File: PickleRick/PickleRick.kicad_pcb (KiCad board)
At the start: 4 copper layers, 100 x 37 mm, 184 parts, among them J1 Conn_01x05_Male, J10 Conn_01x03_Male, J11 Conn_01x03_Male, J12 Conn_01x03_Male, J13 Conn_01x03_Male, J14 DeployLipo, J15 UCLipo, J16 Conn_Coaxial, J17 USB_C_Receptacle_USB2.0, J18 Conn_Coaxial, J2 Conn_01x02_Male, J3 Conn_01x02_Male, J4 Micro_SD_Card_Det, J5 Conn_01x07_Male, Q1 MMDT2222A, Q2 PMV20ENR, Q3 PMV20ENR, Q4 PMV20ENR, Q5 PMV20ENR, Q6 PMV20ENR, U1 SN65HVD230, U10 LTC4411ES5TRMPBF, U11 LTC4411ES5TRMPBF, U12 TPS54233D, U13 LTC4412xS6, U14 LTC4412xS6, U15 LTC4412xS6, U16 LTC4412xS6, U17 MAX-M8Q, U18 CP2102-GMR-QFN28, U19 RFM95W-868S2, U2 ESP32-WROOM-32D, U3 MS5607-02BA, U4 LTV-247, U5 PCA9534RGVR, U6 PCA9685BS, U7 H3LIS100DLTR, U8 ICM-20608-G, U9 MMC5983MA

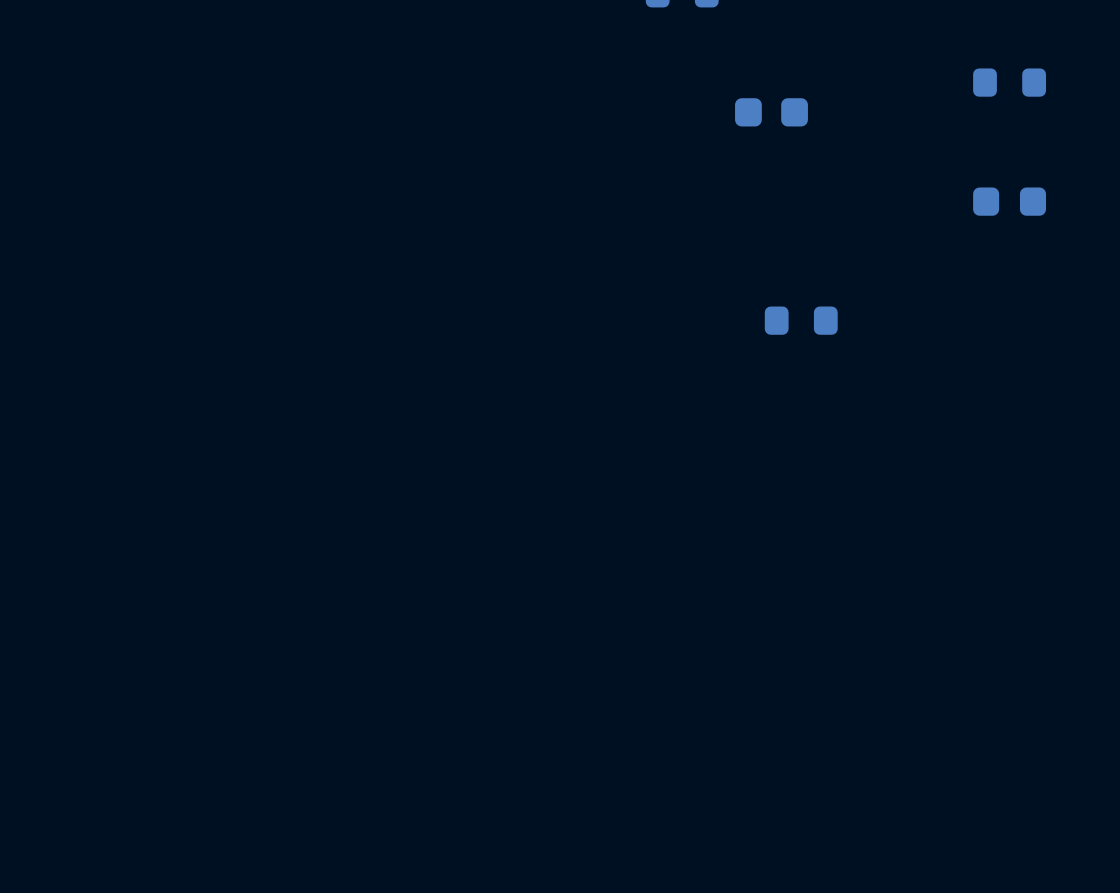
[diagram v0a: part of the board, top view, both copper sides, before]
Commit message: Annotated schematic & done layout for buck converter
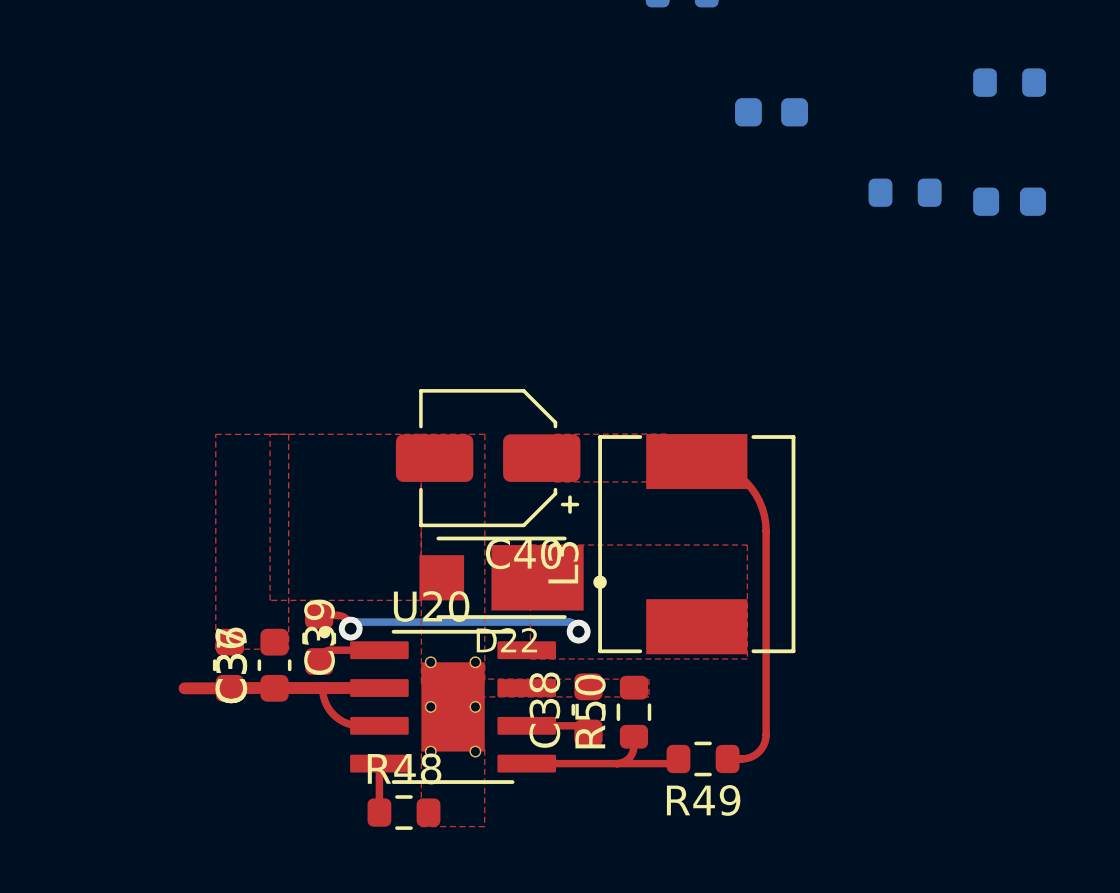
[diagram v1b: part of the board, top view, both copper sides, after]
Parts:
- added C36: 0.1uF, Capacitor_SMD:C_0603_1608Metric, F.Cu at (117.5, 155.4)
- added C37: 10uF, Capacitor_SMD:C_0603_1608Metric, F.Cu at (116.0, 155.4)
- added C38: 22nF, Capacitor_SMD:C_0603_1608Metric, F.Cu at (128.1, 156.9)
- added C39: 0.1uF, Capacitor_SMD:C_0603_1608Metric, F.Cu at (119.0, 154.5)
- added C40: more than 54.2 uF, Capacitor_SMD:CP_Elec_4x5.8, F.Cu at (124.7, 148.4)
- added D22: V8PAM10S, iclr:DIO_V3PAN50-M3_I, F.Cu at (125.1, 152.5)
- added L3: 4.7 uH, iclr:IND_SRP6540-390M, F.Cu at (131.7, 151.3)
- added R48: 49.9k, Resistor_SMD:R_0603_1608Metric, F.Cu at (121.9, 160.4)
- added R49: 64.67k, Resistor_SMD:R_0603_1608Metric, F.Cu at (131.9, 158.6)
- added R50: 10k, Resistor_SMD:R_0603_1608Metric, F.Cu at (129.6, 157.0)
- added U20: LMR14050-Q1, iclr:SOIC127P600X170-9N, F.Cu at (123.5, 156.8)
- moved R38 5.54 mm to (138.7, 139.5)
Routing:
- net +6V: track 0.00 -> 12.1 mm
- net Net-(C39-Pad2): track 0.00 -> 9.52 mm, vias 0 -> 2
- net +24V: track 0.00 -> 9.15 mm
- net /nukes/FB: track 0.00 -> 6.38 mm
- net Net-(C39-Pad1): track 0.00 -> 2.23 mm
- net Net-(C38-Pad1): track 0.00 -> 2.17 mm
- net Net-(R48-Pad1): track 0.00 -> 1.65 mm
- added copper zone on F.Cu, net +6V
- added copper zone on F.Cu, net Net-(C39-Pad2)
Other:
- board text added: "24V IN"

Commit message: first full layout of pickle complete
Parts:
- removed BZ1: Buzzer, Buzzer_Beeper:Buzzer_TDK_PS1240P02BT_D12.2mm_H6.5mm
- removed C40: more than 54.2 uF, Capacitor_SMD:CP_Elec_4x5.8
- removed D13, D14, D7, D9: FIRING, LED_SMD:LED_0603_1608Metric
- removed D22: V8PAM10S, iclr:DIO_V3PAN50-M3_I
- removed G***: LOGO, iclr:iclr_logo
- removed G***: LOGO, iclr:pickle_ric
- removed J13: Conn_01x03_Male, Connector_PinHeader_2.54mm:PinHeader_1x03_P2.54mm_Vertical
- removed L1: PE-92111KNL, Inductor_SMD:L_12x12mm_H6mm
- removed L3: 4.7 uH, iclr:IND_SRP6540-390M
- removed R23, R24, R31, R32: 2K, Resistor_SMD:R_0603_1608Metric
- removed R50: 10k, Resistor_SMD:R_0603_1608Metric
- removed REF**: Write_Pad, iclr:Write_Pad
- removed REF**: Axes_Magnetic_Lefthand_Xdown, iclr:Axes_Magnetic_Lefthand_Xdown
- removed TP1, TP10, TP2, TP29, TP4, TP7, TP9: TestPoint, TestPoint:TestPoint_THTPad_1.0x1.0mm_Drill0.5mm
- removed U20: LMR14050-Q1, iclr:SOIC127P600X170-9N
- added D21: USB_LED, LED_SMD:LED_0603_1608Metric, F.Cu at (168.3, 94.9)
- added J6: Screw_Terminal_01x08, TerminalBlock_TE-Connectivity:TerminalBlock_TE_282834-8_1x08_P2.54mm_Horizontal, F.Cu at (119.5, 62.3)
- added JP1: SolderJumper_2_Open, Jumper:SolderJumper-2_P1.3mm_Open_RoundedPad1.0x1.5mm, F.Cu at (173.9, 65.2)
- added JP2: SolderJumper_2_Open, Jumper:SolderJumper-2_P1.3mm_Open_RoundedPad1.0x1.5mm, B.Cu at (148.0, 66.4)
- added Q10: AO3401A, Package_TO_SOT_SMD:SOT-23, F.Cu at (156.4, 88.1)
- added Q7: SI4143DY-T1-GE3, Package_SO:SOIC-8_3.9x4.9mm_P1.27mm, F.Cu at (136.5, 70.7)
- added Q8: SI4143DY-T1-GE3, Package_SO:SOIC-8_3.9x4.9mm_P1.27mm, F.Cu at (145.9, 71.5)
- added Q9: AO3401A, Package_TO_SOT_SMD:SOT-23, F.Cu at (151.3, 85.3)
- C23: value 10 nF -> 10uF
- C24: value 130pF -> 10uF
- C26: value 130pF -> 100nF
- C27: value 0.1uF -> 160pF
- C28: value 470uF -> 100nF; footprint Capacitor_SMD:CP_Elec_8x6.7 -> Capacitor_SMD:C_0603_1608Metric
- C36: value 0.1uF -> 10uF
- C37: value 10uF -> 0.1uF
- C38: value 22nF -> 220pF
- C39: value 0.1uF -> 220 pF
- D10, D15, D16, D8: footprint Diode_SMD:D_SOD-123F -> Diode_SMD:D_SOD-128
- D19: value B340 -> SM712_SOT23; footprint Diode_SMD:D_SMC -> Package_TO_SOT_SMD:SOT-23
- D6, J5, Q2, R10, R11, R16, R22, R9: moved to B.Cu
- J1: value Conn_01x05_Male -> Conn_01x06_Male; footprint Connector_PinSocket_2.54mm:PinSocket_1x05_P2.54mm_Vertical -> Connector_Molex:Molex_Mini-Fit_Jr_5566-06A_2x03_P4.20mm_Vertical
- J11: value Conn_01x03_Male -> Conn_01x02_Male; footprint Connector_PinHeader_2.54mm:PinHeader_1x03_P2.54mm_Vertical -> Connector_JST:JST_PH_B2B-PH-K_1x02_P2.00mm_Vertical
- J12: value Conn_01x03_Male -> Conn_01x05_Male; footprint Connector_PinHeader_2.54mm:PinHeader_1x03_P2.54mm_Vertical -> Connector_PinHeader_2.54mm:PinHeader_1x05_P2.54mm_Vertical
- J14: footprint TerminalBlock_Phoenix:TerminalBlock_Phoenix_MKDS-1,5-2-5.08_1x02_P5.08mm_Horizontal -> TerminalBlock_Phoenix:TerminalBlock_Phoenix_MKDS-3-2-5.08_1x02_P5.08mm_Horizontal
- J15: footprint TerminalBlock_Phoenix:TerminalBlock_Phoenix_MKDS-1,5-2-5.08_1x02_P5.08mm_Horizontal -> Connector_JST:JST_PH_B2B-PH-K_1x02_P2.00mm_Vertical
- J4, R15: moved to F.Cu
- Q3, Q4, Q5, Q6: value PMV20ENR -> NCV8415STT1G; footprint Package_TO_SOT_SMD:SOT-23 -> Package_TO_SOT_SMD:SOT-223
- R39: value 54.9K -> 90
- R40: value 10K -> 90
- R41: value 1.54K -> 10k
- R48: value 49.9k -> 60
- R49: value 64.67k -> 60
- TP11, TP12, TP13, TP14, TP15, TP16, TP20, TP21, TP22, TP23, TP24, TP25, TP26, TP27, TP28, TP3, TP5, TP6, TP8: footprint TestPoint:TestPoint_THTPad_1.0x1.0mm_Drill0.5mm -> TestPoint:TestPoint_Pad_D1.0mm
- TP17, TP18, TP19, TP30, TP31, TP32: footprint TestPoint:TestPoint_THTPad_1.0x1.0mm_Drill0.5mm -> TestPoint:TestPoint_Pad_D1.0mm; moved to B.Cu
- U12: value TPS54233D -> LT1963AxST-3.3; footprint iclr:SOIC127P599X175-8N -> Package_TO_SOT_SMD:SOT-223-3_TabPin2
- moved TP20 157.7 mm to (187.8, 67.9)
- moved TP8 154.9 mm to (193.8, 90.7)
- moved TP26 153.4 mm to (190.2, 68.1)
- moved TP23 153.2 mm to (183.8, 65.4)
- moved TP25 149.9 mm to (192.3, 68.1)
- moved TP21 148.7 mm to (185.8, 67.9)
- moved D6 143.5 mm to (188.6, 66.0), turned to 90 degrees
- moved TP24 141.2 mm to (183.8, 67.9)
- moved TP3 140.2 mm to (191.3, 66.4)
- moved Q2 138.7 mm to (185.4, 66.5)
- moved TP16 136.9 mm to (171.9, 76.0)
- moved TP14 133.0 mm to (177.2, 83.0)
- moved TP13 133.0 mm to (168.3, 83.7)
- moved TP6 129.8 mm to (188.3, 91.4)
- moved TP15 129.4 mm to (166.5, 84.8)
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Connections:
- net Net-(J14-Pad1) renamed /power/Deploy_Lipo+
- net Net-(J15-Pad1) renamed /power/UC_Lipo+
- C23 pad 1: Net-(C23-Pad1) -> +3V3
- C24 pad 1: Net-(C24-Pad1) -> GND
- C24 pad 2: GND -> /power/3.3reg_in
- C25 pad 1: +24V -> GND
- C25 pad 2: GND -> /power/3.3reg_out
- C26 pad 1: Net-(C24-Pad1) -> GND
- C26 pad 2: Net-(C26-Pad2) -> /power/3.3reg_out
- C27 pad 1: Net-(C27-Pad1) -> GND
- C28 pad 1: +6V -> +3V3
- C36 pad 1: +24V -> +3V3
- C37 pad 1: +24V -> Net-(C37-Pad1)
- C38 pad 1: Net-(C38-Pad1) -> GND
- C38 pad 2: GND -> /CAN_HIGH
- C39 pad 1: Net-(C39-Pad1) -> GND
- C39 pad 2: Net-(C39-Pad2) -> /CAN_LOW
- C7 pad 2: Net-(C7-Pad2) -> GND
- C8 pad 2: Net-(C7-Pad2) -> GND
- D10 pad 2: Net-(D10-Pad2) -> /nukes/Nuke3-
- D11 pad 2: Net-(D11-Pad2) -> /nukes/Nuke1-
- D12 pad 2: Net-(D10-Pad2) -> /nukes/Nuke3-
- D15 pad 2: Net-(D15-Pad2) -> /nukes/Nuke2-
- D16 pad 2: Net-(D16-Pad2) -> /nukes/Nuke4-
- D17 pad 2: Net-(D15-Pad2) -> /nukes/Nuke2-
- D18 pad 2: Net-(D16-Pad2) -> /nukes/Nuke4-
- D19 pad 1: Net-(C27-Pad2) -> /CAN_LOW
- D19 pad 2: GND -> /CAN_HIGH
- D6 pad 2: Net-(BZ1-Pad2) -> Net-(D6-Pad2)
- D8 pad 2: Net-(D11-Pad2) -> /nukes/Nuke1-
- J1 pad 1: /CAN_HIGH -> GND
- J1 pad 3: /power/RBUS_24V_IN -> /power/RBUS_3.3_IN
- J1 pad 4: /power/RBUS_3.3_IN -> /power/RBUS_24V_IN
- J1 pad 5: /CAN_LOW -> /CAN_HIGH
- J10 pad 2: +6V -> /SCL
- J10 pad 3: /nukes/SERVO1 -> /SDA
- J11 pad 1: GND -> Net-(D6-Pad2)
- J11 pad 2: +6V -> +3V3
- J12 pad 2: +6V -> /nukes/SERVO1
- J12 pad 3: /nukes/SERVO3 -> /nukes/SERVO2
- Q3 pad 2: GND -> Net-(D8-Pad1)
- Q3 pad 3: Net-(D8-Pad1) -> GND
- Q4 pad 2: GND -> Net-(D10-Pad1)
- Q4 pad 3: Net-(D10-Pad1) -> GND
- Q5 pad 2: GND -> Net-(D15-Pad1)
- Q5 pad 3: Net-(D15-Pad1) -> GND
- Q6 pad 2: GND -> Net-(D16-Pad1)
- Q6 pad 3: Net-(D16-Pad1) -> GND
- R36 pad 1: Net-(R36-Pad1) -> Net-(U4-Pad1)
- R39 pad 1: Net-(C26-Pad2) -> /CAN_TX
- R39 pad 2: GND -> Net-(C27-Pad2)
- R40 pad 1: +6V -> /CAN_RX
- R40 pad 2: /power/VSENSE -> Net-(R40-Pad2)
- R41 pad 1: /power/VSENSE -> Net-(R41-Pad1)
- R48 pad 1: Net-(R48-Pad1) -> /CAN_HIGH
- R48 pad 2: GND -> Net-(C37-Pad1)
- R49 pad 1: +6V -> Net-(C37-Pad1)
- R49 pad 2: /nukes/FB -> /CAN_LOW
- TP11 pad 1: /HSPI_MISO -> /VSPI_MISO
- TP12 pad 1: /HSPI_MOSI -> /VSPI_MOSI
- TP13 pad 1: /HSPI_SCLK -> /VSPI_SCLK
- TP17 pad 1: /VSPI_SCLK -> /HSPI_SCLK
- TP18 pad 1: /VSPI_MISO -> /HSPI_MISO
- TP19 pad 1: /VSPI_MOSI -> /HSPI_MOSI
- U1 pad 1: /CAN_TX -> Net-(C27-Pad2)
- U1 pad 4: /CAN_RX -> Net-(R40-Pad2)
- U1 pad 5: unconnected-(U1-Pad5) -> /Vref
- U1 pad 8: GND -> Net-(R41-Pad1)
- U12 pad 1: Net-(C27-Pad1) -> /power/3.3reg_in
- U12 pad 2: +24V -> GND
- U12 pad 3: unconnected-(U12-Pad3) -> /power/3.3reg_out
- U13 pad 5: unconnected-(U13-Pad5) -> Net-(Q7-Pad4)
- U13 pad 6: unconnected-(U13-Pad6) -> +24V
- U14 pad 5: unconnected-(U14-Pad5) -> Net-(Q8-Pad4)
- U14 pad 6: unconnected-(U14-Pad6) -> +24V
- U15 pad 5: unconnected-(U15-Pad5) -> Net-(Q9-Pad1)
- U15 pad 6: unconnected-(U15-Pad6) -> /power/3.3reg_in
- U16 pad 5: unconnected-(U16-Pad5) -> Net-(Q10-Pad1)
- U16 pad 6: unconnected-(U16-Pad6) -> /power/3.3reg_in
- U2 pad 12: /BARO_CS -> /Buzzer
- U2 pad 13: /HSPI_SCLK -> /VSPI_SCLK
- U2 pad 14: /HSPI_MISO -> /VSPI_MISO
- U2 pad 16: /HSPI_MOSI -> /VSPI_MOSI
- U2 pad 24: /Buzzer -> /BARO_CS
- U2 pad 30: /VSPI_SCLK -> /HSPI_SCLK
- U2 pad 31: /VSPI_MISO -> /HSPI_MISO
- U2 pad 37: /VSPI_MOSI -> /HSPI_MOSI
- U4 pad 1: Net-(R27-Pad1) -> Net-(U4-Pad1)
- U4 pad 10: /nukes/Cont4 -> /nukes/Cont1
- U4 pad 12: /nukes/Cont3 -> /nukes/Cont2
- U4 pad 14: /nukes/Cont2 -> /nukes/Cont3
- U4 pad 16: /nukes/Cont1 -> /nukes/Cont4
- U4 pad 2: Net-(D11-Pad2) -> /nukes/Nuke4-
- U4 pad 3: Net-(R35-Pad1) -> Net-(R29-Pad1)
- U4 pad 4: Net-(D15-Pad2) -> /nukes/Nuke3-
- U4 pad 5: Net-(R29-Pad1) -> Net-(R35-Pad1)
- U4 pad 6: Net-(D10-Pad2) -> /nukes/Nuke2-
- U4 pad 7: Net-(R36-Pad1) -> Net-(R27-Pad1)
- U4 pad 8: Net-(D16-Pad2) -> /nukes/Nuke1-
- U5 pad 10: /nukes/Nuke4 -> /nukes/Nuke1
- U5 pad 2: /nukes/Cont1 -> /nukes/Cont4
- U5 pad 3: /nukes/Nuke1 -> /nukes/Nuke4
- U5 pad 4: /nukes/Cont2 -> /nukes/Cont3
- U5 pad 5: /nukes/Nuke2 -> /nukes/Nuke3
- U5 pad 7: /nukes/Cont3 -> /nukes/Cont2
- U5 pad 8: /nukes/Nuke3 -> /nukes/Nuke2
- U5 pad 9: /nukes/Cont4 -> /nukes/Cont1
- U6 pad 10: unconnected-(U6-Pad10) -> /nukes/SERVO1
- U6 pad 11: Net-(U6-Pad11) -> GND
- U6 pad 12: unconnected-(U6-Pad12) -> /nukes/SERVO2
- U6 pad 13: unconnected-(U6-Pad13) -> /nukes/SERVO3
- U6 pad 14: unconnected-(U6-Pad14) -> /nukes/SERVO4
- U6 pad 29: Net-(U6-Pad11) -> GND
- U6 pad 3: /nukes/SERVO1 -> unconnected-(U6-Pad3)
- U6 pad 4: /nukes/SERVO2 -> unconnected-(U6-Pad4)
- U6 pad 5: /nukes/SERVO3 -> unconnected-(U6-Pad5)
- U6 pad 6: /nukes/SERVO4 -> unconnected-(U6-Pad6)
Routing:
- net GND: track 0.00 -> 231.2 mm, vias 0 -> 104
- net /SDA: track 2.22 -> 133.4 mm, vias 0 -> 3
- net /SCL: track 2.00 -> 131.0 mm, vias 0 -> 2
- net /LORA_INT: track 0.00 -> 110.3 mm, vias 0 -> 1
- net /SD1_DET: track 1.65 -> 110.6 mm, vias 0 -> 3
- net /SD2_CS: track 0.00 -> 99.3 mm, vias 0 -> 3
- net /SD1_CS: track 1.97 -> 100.3 mm, vias 0 -> 2
- net /HSPI_MOSI: track 0.00 -> 97.4 mm, vias 0 -> 2
- net /VSPI_SCLK: track 3.86 -> 99.9 mm, vias 0 -> 6
- net /SD2_DET: track 0.00 -> 96.0 mm, vias 0 -> 2
- net /VSPI_MOSI: track 9.33 -> 98.9 mm, vias 0 -> 6
- net /VSPI_MISO: track 17.4 -> 105.6 mm, vias 0 -> 6
- net /HSPI_MISO: track 0.00 -> 83.2 mm, vias 0 -> 2
- net +3V3: track 12.6 -> 94.3 mm, vias 0 -> 36
- net /HSPI_SCLK: track 0.00 -> 77.7 mm, vias 0 -> 2
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- added copper zone on F.Cu, net +24V
- added copper zone on In2.Cu, net +3V3
- added copper zone on F.Cu, net /power/Deploy_Lipo+
- added copper zone on F.Cu, net /power/RBUS_24V_IN
- added copper zone on In1.Cu, net GND
- removed copper zone on F.Cu, net +6V
- removed copper zone on F.Cu, net Net-(C39-Pad2)
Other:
- board text removed: "24V IN"

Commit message: pickle layed out
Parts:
- removed D11, D12, D17, D18: CONTINUITY, LED_SMD:LED_0603_1608Metric
- removed R28, R30, R37, R38: 2K, Resistor_SMD:R_0603_1608Metric
- removed TP5: TestPoint, TestPoint:TestPoint_Pad_D1.0mm
- added G***: LOGO, iclr:pickle_ric, B.Cu at (167.7, 77.8)
- added LOGO1: LOGO, iclr:iclr_logo, F.Cu at (129.2, 75.2)
- added REF**: Write_Pad, iclr:Write_Pad, F.Cu at (190.9, 78.0)
- added TP1: TestPoint, TestPoint:TestPoint_Pad_D1.0mm, F.Cu at (170.9, 88.0)
- added TP2: TestPoint, TestPoint:TestPoint_Pad_D1.0mm, F.Cu at (177.4, 95.9)
- moved JP2 19.9 mm to (167.9, 65.3), turned to 90 degrees
- moved J10 11.5 mm to (109.1, 61.9)
- moved TP6 5.90 mm to (194.2, 90.8)
- moved TP22 5.53 mm to (159.1, 83.4)
- moved Q6 3.22 mm to (115.3, 72.9)
- moved R36 3.21 mm to (110.7, 81.0), turned to 0 degrees
- moved R27 2.79 mm to (120.2, 81.0), turned to 0 degrees
- moved R35 2.78 mm to (117.2, 81.0), turned to 0 degrees
- moved TP8 2.51 mm to (191.2, 90.8)
- moved C8 2.43 mm to (122.8, 93.0)
- moved Q3 2.29 mm to (138.8, 72.9)
- moved R29 2.29 mm to (113.7, 81.0)
- moved TP13 2.24 mm to (167.8, 81.5)
- moved D16 2.15 mm to (114.8, 66.1)
- moved D10 2.10 mm to (122.7, 66.2)
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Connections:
- J10 pad 2: /SCL -> /SDA
- J10 pad 3: /SDA -> /SCL
- R36 pad 1: Net-(U4-Pad1) -> Net-(R36-Pad1)
- U4 pad 1: Net-(U4-Pad1) -> /nukes/Nuke4-
- U4 pad 10: /nukes/Cont1 -> +3V3
- U4 pad 11: +3V3 -> /nukes/Cont2
- U4 pad 12: /nukes/Cont2 -> +3V3
- U4 pad 13: +3V3 -> /nukes/Cont3
- U4 pad 14: /nukes/Cont3 -> +3V3
- U4 pad 15: +3V3 -> /nukes/Cont4
- U4 pad 16: /nukes/Cont4 -> +3V3
- U4 pad 2: /nukes/Nuke4- -> Net-(R36-Pad1)
- U4 pad 3: Net-(R29-Pad1) -> /nukes/Nuke3-
- U4 pad 4: /nukes/Nuke3- -> Net-(R29-Pad1)
- U4 pad 5: Net-(R35-Pad1) -> /nukes/Nuke2-
- U4 pad 6: /nukes/Nuke2- -> Net-(R35-Pad1)
- U4 pad 7: Net-(R27-Pad1) -> /nukes/Nuke1-
- U4 pad 8: /nukes/Nuke1- -> Net-(R27-Pad1)
- U4 pad 9: +3V3 -> /nukes/Cont1
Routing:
- net GND: track 231.2 -> 160.7 mm, vias 104 -> 266
- net /nukes/Nuke1: track 1.15 -> 45.2 mm, vias 1 -> 2
- net /SCL: track 131.0 -> 161.3 mm
- net /nukes/Nuke2: track 1.69 -> 30.6 mm, vias 1 -> 2
- net /nukes/Nuke4: track 1.40 -> 28.7 mm, vias 1 -> 2
- net /SDA: track 133.4 -> 159.8 mm
- net /nukes/Nuke3: track 1.43 -> 23.9 mm, vias 1 -> 2
- net /power/Deploy_Lipo+: track 8.00 -> 26.1 mm, vias 0 -> 1
- net /power/UC_Lipo+: track 50.5 -> 36.1 mm
- net /LORA_INT: track 110.3 -> 119.1 mm, vias 1 -> 2
- net /nukes/Nuke1-: track 54.2 -> 62.4 mm
- net /nukes/Nuke2-: track 58.4 -> 53.0 mm
- net Net-(D17-Pad1): track 5.15 -> 0.00 mm
- net +3V3: track 94.3 -> 97.9 mm, vias 36 -> 43
- net Net-(R36-Pad1): track 0.00 -> 2.72 mm
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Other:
- outline, holes or cut-outs redrawn
- board text added: "Designed By Kiran de Silva Electronics & Payload 2022"
- board text added: "Pickle Rick V1.0"

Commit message: pickle update
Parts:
- added R23: 7.5k, Resistor_SMD:R_0603_1608Metric, B.Cu at (170.2, 64.5)
- added R24: 2.4k, Resistor_SMD:R_0603_1608Metric, B.Cu at (170.2, 66.0)
- added R28: 24k, Resistor_SMD:R_0603_1608Metric, B.Cu at (170.2, 92.1)
- added R30: 47k, Resistor_SMD:R_0603_1608Metric, B.Cu at (170.2, 93.6)
- J5: value Conn_01x07_Male -> 292227-7; footprint Connector_JST:JST_GH_SM07B-GHS-TB_1x07-1MP_P1.25mm_Horizontal -> iclr:292227-7
- TP2: moved to B.Cu
- moved R16 19.4 mm to (150.3, 91.6), turned to 0 degrees
- moved R21 10.2 mm to (140.7, 84.8), turned to -90 degrees
- moved J5 7.70 mm to (129.0, 88.3), turned to 0 degrees
- moved R22 4.13 mm to (138.7, 84.8)
- moved TP2 1.32 mm to (176.4, 95.1), turned to 180 degrees
- moved TP23 0.94 mm to (184.3, 65.5)
- moved TP1 0.85 mm to (171.0, 87.2)
- moved R10 0.62 mm to (145.2, 94.2)
- moved R9 0.60 mm to (145.2, 95.7)
- moved JP2 0.53 mm to (167.4, 65.2)
- moved R11 0.50 mm to (145.2, 92.6)
- moved JP1 0.38 mm to (174.0, 65.3)
- moved TP20 0.25 mm to (187.9, 68.1)
- moved TP21 0.25 mm to (185.8, 68.1)
- moved D4 0.24 mm to (144.4, 95.1)
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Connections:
- C31 pad 2: VBUS -> +3V3
- C33 pad 2: VBUS -> +3V3
- J5 pad 1: /SD2_DET -> +3V3
- J5 pad 2: /HSPI_MISO -> /SD2_CS
- J5 pad 3: /HSPI_SCLK -> /HSPI_MOSI
- J5 pad 5: /HSPI_MOSI -> /HSPI_SCLK
- J5 pad 6: /SD2_CS -> /HSPI_MISO
- J5 pad 7: +3V3 -> /SD2_DET
- U18 pad 7: VBUS -> +3V3
- U18 pad 8: VBUS -> Net-(U18-Pad8)
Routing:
- net /BattVolt: track 6.63 -> 29.7 mm, vias 0 -> 1
- net /HSPI_MOSI: track 97.8 -> 88.4 mm
- net /HSPI_MISO: track 82.6 -> 74.7 mm
- net Net-(D4-Pad2): track 8.44 -> 2.28 mm
- net /HSPI_SCLK: track 76.2 -> 70.5 mm
- net VBUS: track 34.8 -> 31.4 mm
- net Net-(U18-Pad8): track 0.00 -> 3.36 mm, vias 0 -> 1
- net +3V3: track 97.9 -> 100.8 mm, vias 43 -> 44
- net /power/UC_Lipo+: track 36.1 -> 38.9 mm
- net /VSPI_MISO: track 103.0 -> 105.4 mm
- net GND: track 160.7 -> 162.7 mm, vias 266 -> 264
- net /SD2_CS: track 100.0 -> 101.8 mm, vias 3 -> 1
- net /LORA_INT: track 119.1 -> 120.4 mm
- net /EN: track 52.3 -> 51.1 mm
- net /SD1_CS: track 100.2 -> 99.3 mm
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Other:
- board text added: "BARO"
- board text added: "BUZZ"
- board text added: "CRX"
- board text added: "CTX"
- board text added: "D+"
- board text added: "D-"
- board text added: "DPWR"
- board text added: "DTR"
- board text added: "EN-BOOT"
- board text added: "H_MISO"
- board text added: "H_MOSI"
- board text added: "H_SCLK"
- board text added: "I2C"
- board text added: "IMU1"
- board text added: "IMU2"
- board text added: "MAG"
- board text added: "PYROS"
- board text added: "RBUS"
- board text added: "RTS"
- board text added: "RX"
- board text added: "RXD"
- board text added: "SD1"
- board text added: "SD2"
- board text added: "SERVO"
- board text added: "SINGLE LIPO"
- board text added: "TERM"
- board text added: "TX"
- board text added: "TXD"
- board text added: "VBUS"
- board text added: "V_MISO"
- board text added: "V_MOSI"
- board text added: "V_SCLK"
- board text added: "uPWR"
